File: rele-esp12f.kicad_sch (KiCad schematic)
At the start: 29 parts, among them J1 N / L_OUT / L_IN, J3 PROG, K1 SRD-05VDC-SL-C, Q1 SS8050, SW1 TS-1187A, SW2 TS-1187A, U1 AMS1117-3.3, U2 ESP-12F

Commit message: v2 redesign: 66.5 x 44 mm board and 110 VAC
  New layout (PS1 and ESP-12F at the top, mains zone at the bottom left
  and low voltage at the bottom right), J3 as a 2x3 header, board nets
  synchronized with the schematic and MAINS/PWR net classes extended to
  the new names, GND planes on both sides restricted to the low-voltage
  zone. BOM, CPL, gerbers, renders and README updated.
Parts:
- D3: LCSC C72043 -> C51933294
- J3: footprint Connector_PinHeader_2.54mm:PinHeader_1x06_P2.54mm_Vertical -> Connector_PinHeader_2.54mm:PinHeader_2x03_P2.54mm_Vertical
- R9: value 1k -> 220; LCSC C21190 -> C22962
- RV1: value 07D471K -> 07D221K
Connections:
- net L_F: now also F1.2; no longer F1.1
- net L_IN: now also F1.1, J1.3 (Pin_3); no longer F1.2, J1.2 (Pin_2)
- net L_OUT: now also J1.2 (Pin_2); no longer J1.3 (Pin_3)

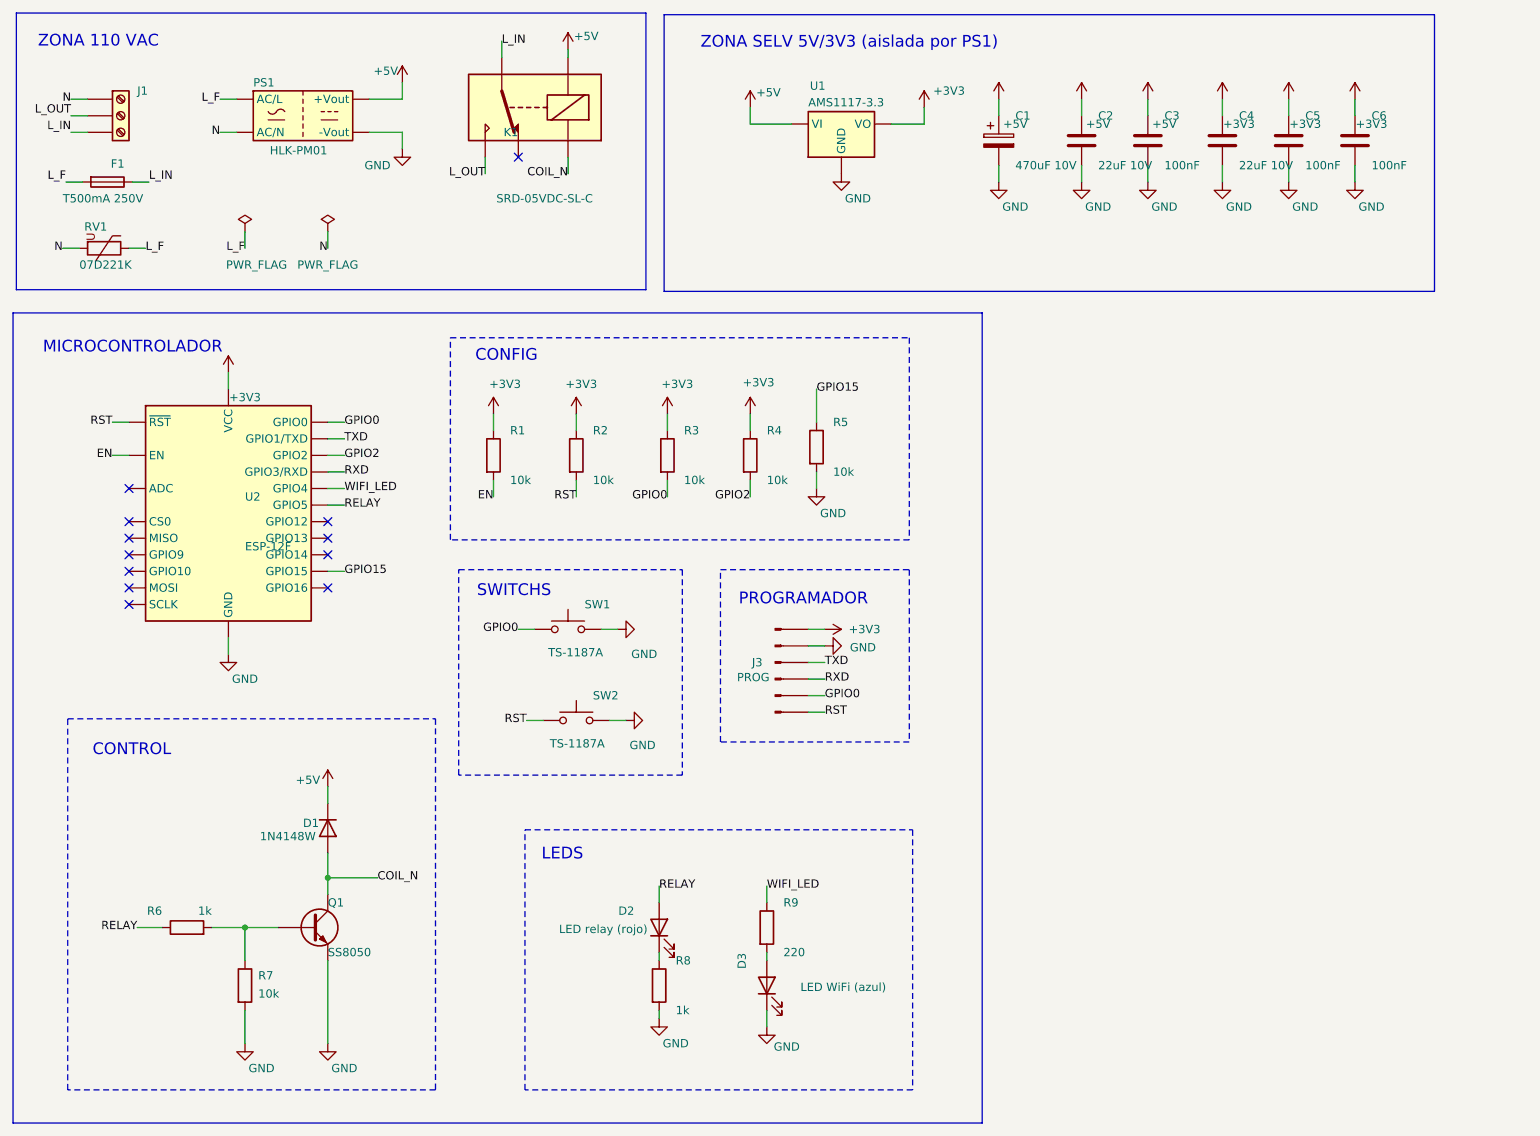
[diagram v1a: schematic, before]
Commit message: v3 revision: Omron G5RL relay, 10 A load and complete documentation
  Hardware
  - Omron G5RL-1A-E-HR relay (16 A, reinforced insulation) instead of
    the SRD-05VDC; 66.5 x 49 mm board.
  - Power path duplicated on both sides (2 x 2.5 mm) for 10 A.
  - J3 powered at 5 V; RC delay on EN/RST (C7, C8) and 10 uF
    decoupling next to the ESP-12F (C9).
  - Mains copper >= 2.0 mm from the edge; K1 rule removed so the 4 mm
    mains/low-voltage clearance applies across the whole board.
  - Gerbers, drill files, BOM, CPL, renders and schematic regenerated.
  
  Repository
  - Restructured README, CHANGELOG and CERN-OHL-W-2.0 license.
  - PDF datasheet and user guide with its generator script.
  - 3D-printable enclosure (FreeCAD, STEP and STL).
  - Relay STEP model and datasheets of the key components.
  - Removed the v1 generator scripts and the empty manual BOM.
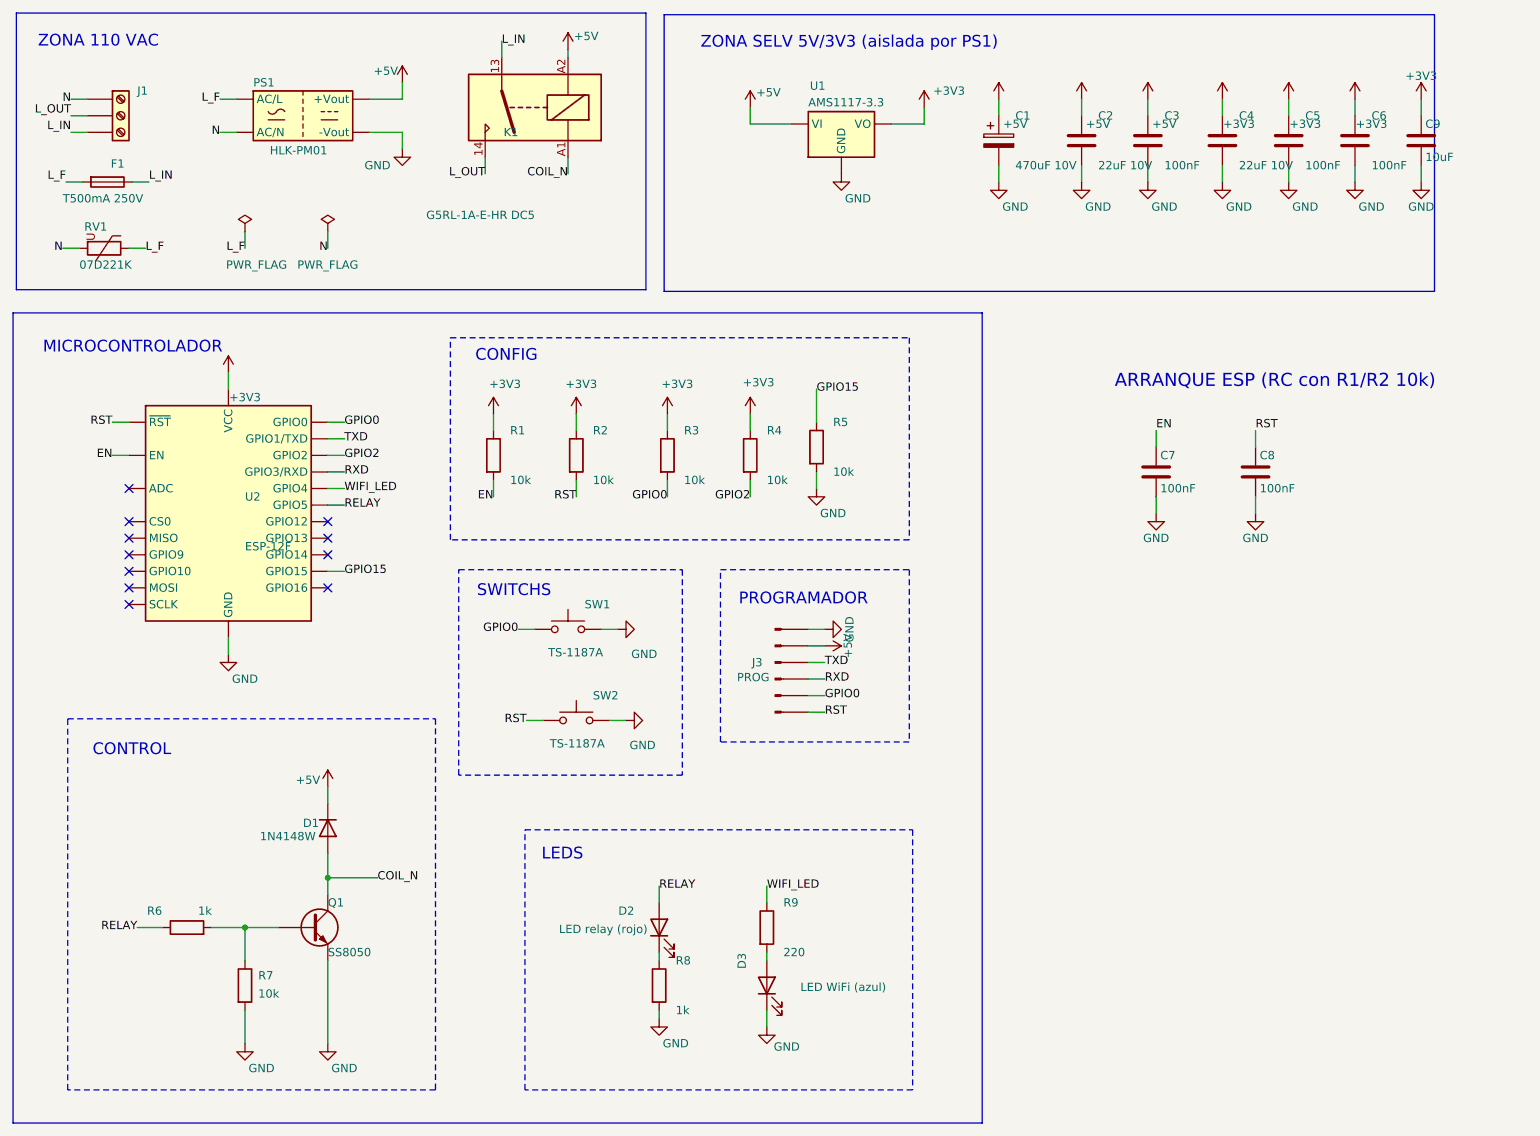
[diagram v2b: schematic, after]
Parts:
- added C7, C8: 100nF, Capacitor_SMD:C_0603_1608Metric, symbol Device:C
- added C9: 10uF, Capacitor_SMD:C_0603_1608Metric, symbol Device:C
- C1: LCSC (none) -> C112505; Montaje Mano -> JLCPCB
- F1: LCSC (none) -> C2762401; Montaje Mano -> JLCPCB
- J1: LCSC (none) -> C72334; Montaje Mano -> JLCPCB
- J3: LCSC (none) -> C65114; Montaje No montar -> JLCPCB
- K1: value SRD-05VDC-SL-C -> G5RL-1A-E-HR DC5; footprint Relay_THT:Relay_SPDT_SANYOU_SRD_Series_Form_C -> Relay_THT:Relay_SPST_Omron_G2RL-1A-E; symbol Relay:SANYOU_SRD_Form_C -> Relay:G2RL-1A-E; LCSC (none) -> C113250; Montaje Mano -> JLCPCB
- PS1: LCSC (none) -> C209903; Montaje Mano -> JLCPCB
- RV1: LCSC (none) -> C49072913; Montaje Mano -> JLCPCB
- U2: LCSC (none) -> C82891; Montaje Mano -> JLCPCB
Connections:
- net +3V3: now also C9.1; no longer J3.1 (Pin_1)
- net +5V: now also J3.2 (Pin_2), K1.A2; no longer K1.2
- net COIL_N: now also K1.A1; no longer K1.5
- net EN: now also C7.1
- net GND: now also J3.1 (Pin_1), C7.2, C8.2, C9.2; no longer J3.2 (Pin_2)
- net L_IN: now also K1.13; no longer K1.1
- net L_OUT: now also K1.14; no longer K1.3
- net RST: now also C8.1
- no-connect marks 12 -> 11
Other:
- note added: "ARRANQUE ESP (RC con R1/R2 10k)"

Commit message: Translate the repository to English
- README, CHANGELOG and enclosure README rewritten in English.
- Folders and files renamed: fabrication/, enclosure/, docs/schematic.pdf,
  docs/pcb_top.png, docs/pcb_bottom.png, scripts/generate_datasheet.py.
- Datasheet and user guide regenerated in English (document rev. B).
- Silkscreen "DANGER: 110 VAC", schematic notes, LED values, design rule
  names and the "Assembly" field translated; schematic title block set
  to revision v3. Gerbers, ZIP, renders and schematic PDF regenerated.
- Enclosure script translated and lid label changed to "RELAY"; STL,
  STEP, FreeCAD document and renders regenerated.

DRC: 0 errors, 0 unconnected (29 warnings, unchanged). ERC: 0 errors.
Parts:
- C1, C2, C3, C4, C5, C6, C7, C8, C9, D1, F1, J1, J3, K1, PS1, Q1, R1, R2, R3, R4, R5, R6, R7, R8, R9, RV1, SW1, SW2, U1, U2: Assembly (none) -> JLCPCB; Montaje JLCPCB -> (none)
- D2: value LED relay (rojo) -> LED relay (red); Assembly (none) -> JLCPCB; Montaje JLCPCB -> (none)
- D3: value LED WiFi (azul) -> LED WiFi (blue); Assembly (none) -> JLCPCB; Montaje JLCPCB -> (none)
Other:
- note added: "110 VAC ZONE"
- note added: "ESP BOOT (RC with R1/R2 10k)"
- note added: "MICROCONTROLLER"
- note added: "PROGRAMMER"
- note added: "SELV ZONE 5V/3V3 (isolated by PS1)"
- note added: "SWITCHES"
- note removed: "ARRANQUE ESP (RC con R1/R2 10k)"
- note removed: "MICROCONTROLADOR"
- note removed: "PROGRAMADOR"
- note removed: "SWITCHS"
- note removed: "ZONA 110 VAC"
- note removed: "ZONA SELV 5V/3V3 (aislada por PS1)"
- title: Modulo rele Wi-Fi ESP-12F 110 VAC -> Wi-Fi Relay Module ESP-12F 110 VAC
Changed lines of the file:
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@@
 	(paper "A4")
 	(title_block
-		(title "Modulo rele Wi-Fi ESP-12F 110 VAC")
-		(date "2026-09-25")
-		(rev "1.1")
+		(title "Wi-Fi Relay Module ESP-12F 110 VAC")
+		(date "2026-10-03")
+		(rev "v3")
 		(company "@techmigue")
-		(comment 1 "ESP-01S_Relay_Module")
+		(comment 1 "Inspired by aman983/ESP-01S_Relay_Module (new design)")
 		(comment 2 "Hardware: CERN-OHL-W v2")
 	)
@@
 		)
 	)
-	(text "PROGRAMADOR\n"
+	(text "PROGRAMMER\n"
 		(at 126.492 104.648 0)
 		(effects
@@
 		)
 	)
-	(text "MICROCONTROLADOR"
+	(text "MICROCONTROLLER"
 		(at 19.812 66.04 0)
 		(effects
@@
 		)
 	)
-	(text "ZONA 110 VAC\n"
+	(text "110 VAC ZONE\n"
 		(at 19.05 19.13 0)
 		(effects
@@
 		)
 	)
-	(text "ZONA SELV 5V/3V3 (aislada por PS1)"
+	(text "SELV ZONE 5V/3V3 (isolated by PS1)"
 		(at 120.65 19.304 0)
 		(effects
@@
 		)
 	)
-	(text "SWITCHS\n"
+	(text "SWITCHES\n"
 		(at 86.36 103.378 0)
 		(effects
@@
 		)
 	)
-	(text "ARRANQUE ESP (RC con R1/R2 10k)"
+	(text "ESP BOOT (RC with R1/R2 10k)"
 		(at 184.15 72.39 0)
 		(effects
@@
 			)
 		)
-		(property "Montaje" "JLCPCB"
+		(property "Assembly" "JLCPCB"
 			(at 189.23 34.29 0)
 			(hide yes)
@@
 			)
 		)
-		(property "Montaje" "JLCPCB"
+		(property "Assembly" "JLCPCB"
 			(at 166.37 34.29 0)
 			(hide yes)
@@
 			)
 		)
-		(property "Montaje" "JLCPCB"
+		(property "Assembly" "JLCPCB"
 			(at 101.6 82.55 0)
 			(hide yes)
@@
 			)
 		)
-		(property "Montaje" "JLCPCB"
+		(property "Assembly" "JLCPCB"
 			(at 88.9 82.55 0)
 			(hide yes)
@@
 			)
 		)
-		(property "Montaje" "JLCPCB"
+		(property "Assembly" "JLCPCB"
 			(at 29.718 40.64 0)
 			(hide yes)
@@
 			)
 		)
-		(property "Montaje" "JLCPCB"
+		(property "Assembly" "JLCPCB"
 			(at 100.33 109.22 0)
 			(hide yes)
@@
 			)
 		)
-		(property "Montaje" "JLCPCB"
+		(property "Assembly" "JLCPCB"
 			(at 179.07 34.29 0)
 			(hide yes)
@@
 			)
 		)
-		(property "Value" "LED WiFi (azul)"
+		(property "Value" "LED WiFi (blue)"
 			(at 149.098 164.084 90)
 			(show_name no)
@@
 			)
 		)
-		(property "Montaje" "JLCPCB"
+		(property "Assembly" "JLCPCB"
 			(at 130.81 163.83 0)
 			(hide yes)
@@
 			)
 		)
-		(property "Value" "LED relay (rojo)"
+		(property "Value" "LED relay (red)"
 			(at 112.522 155.194 90)
 			(show_name no)
@@
 			)
 		)
-		(property "Montaje" "JLCPCB"
+		(property "Assembly" "JLCPCB"
 			(at 114.3 154.94 0)
 			(hide yes)
@@
 			)
 		)
-		(property "Montaje" "JLCPCB"
+		(property "Assembly" "JLCPCB"
 			(at 130.81 154.94 0)
 			(hide yes)
@@
 			)
 		)
-		(property "Montaje" "JLCPCB"
+		(property "Assembly" "JLCPCB"
 			(at 210.82 34.29 0)
 			(hide yes)
@@
 			)
 		)
-		(property "Description" "Relé SPST-NO 16 A 250 VAC, bobina 5 V, alta corriente de arranque (HR)"
+		(property "Description" "Relay SPST-NO 16 A 250 VAC, 5 V coil, high inrush current (HR)"
 			(at 95.25 29.21 0)
 			(hide yes)
@@
 			)
 		)
-		(property "Montaje" "JLCPCB"
+		(property "Assembly" "JLCPCB"
 			(at 95.25 29.21 0)
 			(hide yes)
@@
 			)
 		)
-		(property "Montaje" "JLCPCB"
+		(property "Assembly" "JLCPCB"
 			(at 63.5 139.7 0)
 			(hide yes)
@@
 			)
 		)
-		(property "Montaje" "JLCPCB"
+		(property "Assembly" "JLCPCB"
 			(at 48.26 92.71 0)
 			(hide yes)
@@
 			)
 		)
-		(property "Montaje" "JLCPCB"
+		(property "Assembly" "JLCPCB"
 			(at 60.96 154.94 0)
 			(hide yes)
@@
 			)
 		)
-		(property "Montaje" "JLCPCB"
+		(property "Assembly" "JLCPCB"
 			(at 50.8 163.83 0)
 			(hide yes)
@@
 			)
 		)
-		(property "Montaje" "JLCPCB"
+		(property "Assembly" "JLCPCB"
 			(at 128.27 82.55 0)
 			(hide yes)
@@
 			)
 		)
-		(property "Montaje" "JLCPCB"
+		(property "Assembly" "JLCPCB"
 			(at 41.91 154.94 0)
 			(hide yes)
@@
 			)
 		)
-		(property "Montaje" "JLCPCB"
+		(property "Assembly" "JLCPCB"
 			(at 59.69 30.48 0)
 			(hide yes)
@@
 			)
 		)
-		(property "Montaje" "JLCPCB"
+		(property "Assembly" "JLCPCB"
 			(at 220.98 34.29 0)
 			(hide yes)
@@
 			)
 		)
-		(property "Montaje" "JLCPCB"
+		(property "Assembly" "JLCPCB"
 			(at 114.3 163.83 0)
 			(hide yes)
@@
 			)
 		)
-		(property "Montaje" "JLCPCB"
+		(property "Assembly" "JLCPCB"
 			(at 138.43 81.28 0)
 			(hide yes)
@@
 			)
 		)
-		(property "Montaje" "JLCPCB"
+		(property "Assembly" "JLCPCB"
 			(at 29.21 50.8 0)
 			(hide yes)
@@
 			)
 		)
-		(property "Montaje" "JLCPCB"
+		(property "Assembly" "JLCPCB"
 			(at 132.08 114.3 0)
 			(hide yes)
@@
 			)
 		)
-		(property "Montaje" "JLCPCB"
+		(property "Assembly" "JLCPCB"
 			(at 101.6 123.19 0)
 			(hide yes)
@@
 			)
 		)
-		(property "Montaje" "JLCPCB"
+		(property "Assembly" "JLCPCB"
 			(at 31.75 30.48 0)
 			(hide yes)
@@
 			)
 		)
-		(property "Montaje" "JLCPCB"
+		(property "Assembly" "JLCPCB"
 			(at 200.66 34.29 0)
 			(hide yes)
@@
 			)
 		)
-		(property "Montaje" "JLCPCB"
+		(property "Assembly" "JLCPCB"
 			(at 115.57 82.55 0)
 			(hide yes)
@@
 			)
 		)
-		(property "Montaje" "JLCPCB"
+		(property "Assembly" "JLCPCB"
 			(at 142.24 31.75 0)
 			(hide yes)
@@
 			)
 		)
-		(property "Montaje" "JLCPCB"
+		(property "Assembly" "JLCPCB"
 			(at 190.5 85.09 0)
 			(hide yes)
@@
 			)
 		)
-		(property "Montaje" "JLCPCB"
+		(property "Assembly" "JLCPCB"
 			(at 205.74 85.09 0)
 			(hide yes)
@@
 			)
 		)
-		(property "Montaje" "JLCPCB"
+		(property "Assembly" "JLCPCB"
 			(at 231.14 34.29 0)
 			(hide yes)
